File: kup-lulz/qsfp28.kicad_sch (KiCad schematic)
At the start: 33 parts, among them J15 CONN_QSFP_HOST, J16 CONN_QSFP_HOST, J35 QSFP_CAGE, J36 QSFP_CAGE, U9 XILINX_ULTRASCALEPLUS_B676

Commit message: Continued initial work on kup-lulz devboard
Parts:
- C81, C82: footprint (none) -> azonenberg_pcb:EIA_0402_CAP_NOSILK
- TP18, TP19, TP20, TP21, TP22, TP23: footprint (none) -> azonenberg_pcb:CONN_U.FL_TE_1909763-1
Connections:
- net QSFP28A_REFCLK0_N: no longer names the net of U9.K6 (MGTREFCLK0N_227)
- net QSFP28A_REFCLK0_P: no longer names the net of U9.K7 (MGTREFCLK0P_227)
- net QSFP28B_REFCLK0_N: no longer names the net of U9.P6 (MGTREFCLK0N_226)
- net QSFP28B_REFCLK0_P: no longer names the net of U9.P7 (MGTREFCLK0P_226)
- net QSFP28B_REFCLK1_N: no longer names the net of U9.M6 (MGTREFCLK1N_226)
- net QSFP28B_REFCLK1_P: no longer names the net of U9.M7 (MGTREFCLK1P_226)
- no-connect marks 0 -> 6
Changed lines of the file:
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@@
   (title_block
     (title "Kintex Ultrascale+ OshPark For The Lulz")
-    (date "2024-01-31")
+    (date "2024-02-01")
     (rev "0.1")
   )
@@
   (junction (at 48.26 135.89) (diameter 0) (color 0 0 0 0)
   )
+  (no_connect (at 138.43 26.67))
+  (no_connect (at 138.43 29.21))
+  (no_connect (at 48.26 19.05))
+  (no_connect (at 138.43 19.05))
+  (no_connect (at 48.26 21.59))
+  (no_connect (at 138.43 21.59))
   (wire (pts (xy 138.43 129.54) (xy 138.43 132.08))
     (stroke (width 0) (type default) (color 0 0 0 0))
@@
     (effects (font (size 1.27 1.27)) (justify left))
   )
-  (hierarchical_label "QSFP28B_REFCLK1_N" (shape input) (at 138.43 29.21 180)
-    (effects (font (size 1.27 1.27)) (justify right))
-  )
   (hierarchical_label "QSFP0_RST_N" (shape input) (at 78.74 135.89 0)
     (effects (font (size 1.27 1.27)) (justify left))
@@
     (effects (font (size 1.27 1.27)) (justify left))
   )
-  (hierarchical_label "QSFP28B_REFCLK1_P" (shape input) (at 138.43 26.67 180)
-    (effects (font (size 1.27 1.27)) (justify right))
-  )
   (hierarchical_label "QSFP28A_REFCLK1_P" (shape input) (at 48.26 26.67 180)
     (effects (font (size 1.27 1.27)) (justify right))
   )
-  (hierarchical_label "QSFP28B_REFCLK0_P" (shape input) (at 138.43 19.05 180)
-    (effects (font (size 1.27 1.27)) (justify right))
-  )
-  (hierarchical_label "QSFP28A_REFCLK0_P" (shape input) (at 48.26 19.05 180)
-    (effects (font (size 1.27 1.27)) (justify right))
-  )
   (hierarchical_label "QSFP_I2C_SDA" (shape bidirectional) (at 78.74 123.19 0)
     (effects (font (size 1.27 1.27)) (justify left))
   )
-  (hierarchical_label "QSFP28B_REFCLK0_N" (shape input) (at 138.43 21.59 180)
-    (effects (font (size 1.27 1.27)) (justify right))
-  )
   (hierarchical_label "GND" (shape input) (at 54.61 212.09 180)
     (effects (font (size 1.27 1.27)) (justify right))
@@
   (hierarchical_label "QSFP0_I2C_SEL_N" (shape input) (at 78.74 133.35 0)
     (effects (font (size 1.27 1.27)) (justify left))
-  )
-  (hierarchical_label "QSFP28A_REFCLK0_N" (shape input) (at 48.26 21.59 180)
-    (effects (font (size 1.27 1.27)) (justify right))
   )
   (hierarchical_label "QSFP1_LPMODE" (shape input) (at 168.91 129.54 0)
@@
       (effects (font (size 1.27 1.27)) (justify left))
     )
-    (property "Footprint" "" (id 2) (at 130.81 204.47 0)
+    (property "Footprint" "azonenberg_pcb:CONN_U.FL_TE_1909763-1" (id 2) (at 130.81 204.47 0)
       (effects (font (size 1.27 1.27)) hide)
     )
@@
       (effects (font (size 1.27 1.27)) (justify left))
     )
-    (property "Footprint" "" (id 2) (at 130.81 256.54 0)
+    (property "Footprint" "azonenberg_pcb:CONN_U.FL_TE_1909763-1" (id 2) (at 130.81 256.54 0)
       (effects (font (size 1.27 1.27)) hide)
     )
@@
       (effects (font (size 1.27 1.27)) (justify left))
     )
-    (property "Footprint" "" (id 2) (at 130.81 269.24 0)
+    (property "Footprint" "azonenberg_pcb:CONN_U.FL_TE_1909763-1" (id 2) (at 130.81 269.24 0)
       (effects (font (size 1.27 1.27)) hide)
     )
@@
       (effects (font (size 1.27 1.27)) (justify left))
     )
-    (property "Footprint" "" (id 2) (at 130.81 229.87 0)
+    (property "Footprint" "azonenberg_pcb:CONN_U.FL_TE_1909763-1" (id 2) (at 130.81 229.87 0)
       (effects (font (size 1.27 1.27)) hide)
     )
@@
       (effects (font (size 1.27 1.27)) (justify left))
     )
-    (property "Footprint" "" (id 2) (at 68.2752 212.09 0)
+    (property "Footprint" "azonenberg_pcb:EIA_0402_CAP_NOSILK" (id 2) (at 68.2752 212.09 0)
       (effects (font (size 1.27 1.27)) hide)
     )
@@
       (effects (font (size 1.27 1.27)) (justify left))
     )
-    (property "Footprint" "" (id 2) (at 68.2752 251.46 0)
+    (property "Footprint" "azonenberg_pcb:EIA_0402_CAP_NOSILK" (id 2) (at 68.2752 251.46 0)
       (effects (font (size 1.27 1.27)) hide)
     )
@@
       (effects (font (size 1.27 1.27)) (justify left))
     )
-    (property "Footprint" "" (id 2) (at 130.81 217.17 0)
+    (property "Footprint" "azonenberg_pcb:CONN_U.FL_TE_1909763-1" (id 2) (at 130.81 217.17 0)
       (effects (font (size 1.27 1.27)) hide)
     )
@@
       (effects (font (size 1.27 1.27)) (justify left))
     )
-    (property "Footprint" "" (id 2) (at 130.81 243.84 0)
-      (effects (font (size 1.27 1.27)) hide)
-    )
+    (property "Footprint" "azonenberg_pcb:CONN_U.FL_TE_1909763-1" (id 2) (at 130.81 243.84 0)
+      (effects (font (size 1.27 1.27)) hide)
+    )

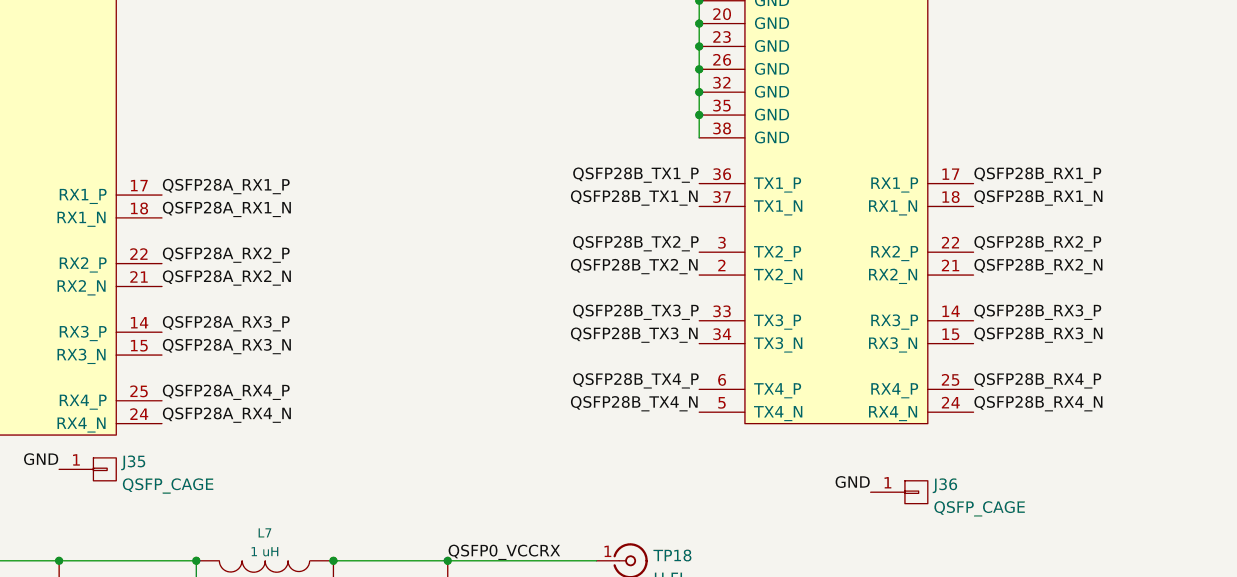
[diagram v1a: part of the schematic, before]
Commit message: Continued initial layout of kup-lulz
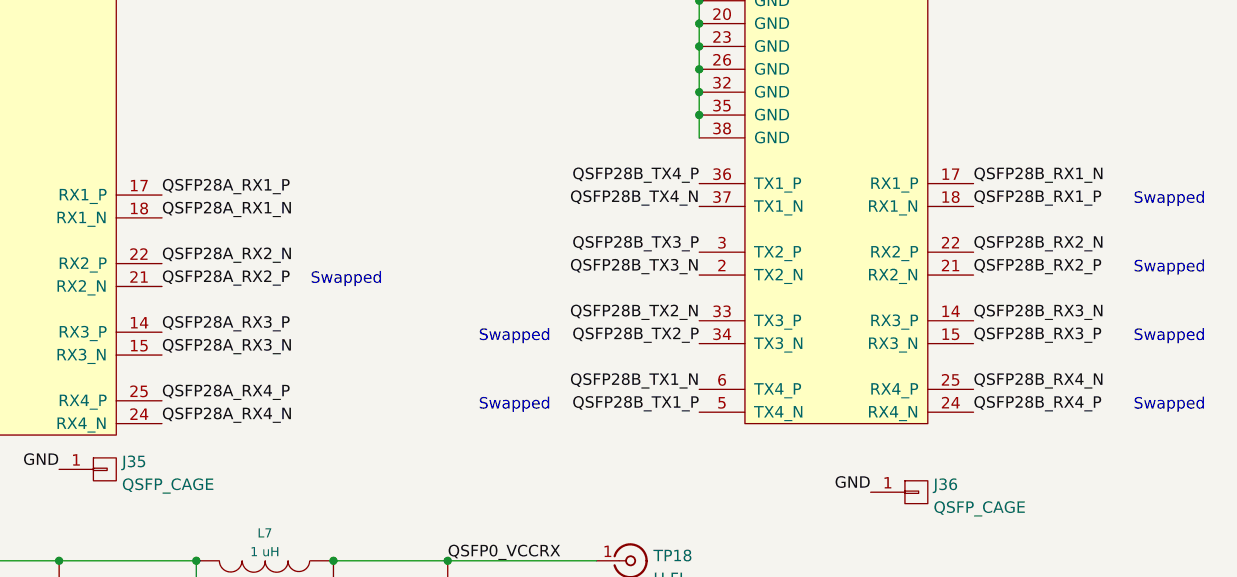
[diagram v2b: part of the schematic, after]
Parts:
- C79, C80, C83, C84, C85, C86, C87, C88: footprint (none) -> azonenberg_pcb:EIA_1210_CAP_NOSILK
- J15, J16: footprint azonenberg_pcb:CONN_QSFP+_TE_2110819-1 -> azonenberg_pcb:CONN_ZQSFP+_TE_1551920-2
- J35, J36: footprint azonenberg_pcb:CONN_QSFP_CAGE_TE_2110487-1 -> azonenberg_pcb:CONN_ZQSFP+_CAGE_TE_4-2170705-5
- L10, L11, L12, L7, L8, L9: footprint (none) -> azonenberg_pcb:EIA_0805_INDUCTOR_NOSILK
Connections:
- net QSFP28A_RX2_N: now also J15.22 (RX2_P); no longer J15.21 (RX2_N)
- net QSFP28A_RX2_P: now also J15.21 (RX2_N); no longer J15.22 (RX2_P)
- net QSFP28B_RX1_N: now also J16.17 (RX1_P); no longer J16.18 (RX1_N)
- net QSFP28B_RX1_P: now also J16.18 (RX1_N); no longer J16.17 (RX1_P)
- net QSFP28B_RX2_N: now also J16.22 (RX2_P); no longer J16.21 (RX2_N)
- net QSFP28B_RX2_P: now also J16.21 (RX2_N); no longer J16.22 (RX2_P)
- net QSFP28B_RX3_N: now also J16.14 (RX3_P); no longer J16.15 (RX3_N)
- net QSFP28B_RX3_P: now also J16.15 (RX3_N); no longer J16.14 (RX3_P)
- net QSFP28B_RX4_N: now also J16.25 (RX4_P); no longer J16.24 (RX4_N)
- net QSFP28B_RX4_P: now also J16.24 (RX4_N); no longer J16.25 (RX4_P)
- net QSFP28B_TX1_N: now also J16.6 (TX4_P); no longer J16.37 (TX1_N)
- net QSFP28B_TX1_P: now also J16.5 (TX4_N); no longer J16.36 (TX1_P)
- net QSFP28B_TX2_N: now also J16.33 (TX3_P); no longer J16.2 (TX2_N)
- net QSFP28B_TX2_P: now also J16.34 (TX3_N); no longer J16.3 (TX2_P)
- net QSFP28B_TX3_N: now also J16.2 (TX2_N); no longer J16.34 (TX3_N)
- net QSFP28B_TX3_P: now also J16.3 (TX2_P); no longer J16.33 (TX3_P)
- net QSFP28B_TX4_N: now also J16.37 (TX1_N); no longer J16.5 (TX4_N)
- net QSFP28B_TX4_P: now also J16.36 (TX1_P); no longer J16.6 (TX4_P)
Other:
- note added: "Swapped"
- company: (none) -> Antikernel Labs

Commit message: Continued initial layout
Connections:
- net QSFP28A_RX1_N: now also J15.22 (RX2_P); no longer J15.18 (RX1_N)
- net QSFP28A_RX1_P: now also J15.21 (RX2_N); no longer J15.17 (RX1_P)
- net QSFP28A_RX2_N: now also J15.17 (RX1_P); no longer J15.22 (RX2_P)
- net QSFP28A_RX2_P: now also J15.18 (RX1_N); no longer J15.21 (RX2_N)
- net QSFP28B_TX3_N: now also J16.3 (TX2_P); no longer J16.2 (TX2_N)
- net QSFP28B_TX3_P: now also J16.2 (TX2_N); no longer J16.3 (TX2_P)
- net QSFP28B_TX4_N: now also J16.36 (TX1_P); no longer J16.37 (TX1_N)
- net QSFP28B_TX4_P: now also J16.37 (TX1_N); no longer J16.36 (TX1_P)
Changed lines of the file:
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@@
     (stroke (width 0) (type default) (color 0 0 0 0))
   )
+  (text "Swapped" (at 121.92 165.1 180)
+    (effects (font (size 1.27 1.27)) (justify right bottom))
+  )
+  (text "Swapped" (at 121.92 172.72 180)
+    (effects (font (size 1.27 1.27)) (justify right bottom))
+  )
   (text "Swapped" (at 186.69 172.72 0)
     (effects (font (size 1.27 1.27)) (justify left bottom))
@@
     (effects (font (size 1.27 1.27)) (justify left bottom))
   )
+  (text "Swapped" (at 95.25 166.37 0)
+    (effects (font (size 1.27 1.27)) (justify left bottom))
+  )
   (text "Swapped" (at 121.92 180.34 180)
     (effects (font (size 1.27 1.27)) (justify right bottom))
@@
     (effects (font (size 1.27 1.27)) (justify left bottom))
   )
-  (label "QSFP28A_RX1_P" (at 78.74 163.83 0)
+  (label "QSFP28A_RX1_P" (at 78.74 173.99 0)
     (effects (font (size 1.27 1.27)) (justify left bottom))
   )
@@
     (effects (font (size 1.27 1.27)) (justify right bottom))
   )
-  (label "QSFP28A_RX2_N" (at 78.74 171.45 0)
+  (label "QSFP28A_RX2_N" (at 78.74 163.83 0)
     (effects (font (size 1.27 1.27)) (justify left bottom))
   )
@@
     (effects (font (size 1.27 1.27)) (justify left bottom))
   )
-  (label "QSFP28B_TX4_N" (at 138.43 165.1 180)
-    (effects (font (size 1.27 1.27)) (justify right bottom))
-  )
-  (label "QSFP28A_RX2_P" (at 78.74 173.99 0)
+  (label "QSFP28B_TX4_N" (at 138.43 162.56 180)
+    (effects (font (size 1.27 1.27)) (justify right bottom))
+  )
+  (label "QSFP28A_RX2_P" (at 78.74 166.37 0)
     (effects (font (size 1.27 1.27)) (justify left bottom))
   )
@@
     (effects (font (size 1.27 1.27)) (justify right bottom))
   )
-  (label "QSFP28B_TX3_N" (at 138.43 172.72 180)
+  (label "QSFP28B_TX3_N" (at 138.43 170.18 180)
     (effects (font (size 1.27 1.27)) (justify right bottom))
   )
@@
     (effects (font (size 1.27 1.27)) (justify right bottom))
   )
-  (label "QSFP28A_RX1_N" (at 78.74 166.37 0)
+  (label "QSFP28A_RX1_N" (at 78.74 171.45 0)
     (effects (font (size 1.27 1.27)) (justify left bottom))
   )
@@
     (effects (font (size 1.27 1.27)) (justify right bottom))
   )
-  (label "QSFP28B_TX3_P" (at 138.43 170.18 180)
+  (label "QSFP28B_TX3_P" (at 138.43 172.72 180)
     (effects (font (size 1.27 1.27)) (justify right bottom))
   )
@@
     (effects (font (size 1.27 1.27)) (justify right bottom))
   )
-  (label "QSFP28B_TX4_P" (at 138.43 162.56 180)
-    (effects (font (size 1.27 1.27)) (justify right bottom))
-  )
+  (label "QSFP28B_TX4_P" (at 138.43 165.1 180)
+    (effects (font (size 1.27 1.27)) (justify right bottom))
+  )

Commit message: Continued initial routing
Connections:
- net QSFP28A_RX2_N: now also J15.18 (RX1_N); no longer J15.17 (RX1_P)
- net QSFP28A_RX2_P: now also J15.17 (RX1_P); no longer J15.18 (RX1_N)
- net QSFP28A_RX3_N: now also J15.25 (RX4_P); no longer J15.15 (RX3_N)
- net QSFP28A_RX3_P: now also J15.24 (RX4_N); no longer J15.14 (RX3_P)
- net QSFP28A_RX4_N: now also J15.15 (RX3_N); no longer J15.24 (RX4_N)
- net QSFP28A_RX4_P: now also J15.14 (RX3_P); no longer J15.25 (RX4_P)
- net QSFP28A_TX2_N: now also J15.33 (TX3_P); no longer J15.2 (TX2_N)
- net QSFP28A_TX2_P: now also J15.34 (TX3_N); no longer J15.3 (TX2_P)
- net QSFP28A_TX3_N: now also J15.6 (TX4_P); no longer J15.34 (TX3_N)
- net QSFP28A_TX3_P: now also J15.5 (TX4_N); no longer J15.33 (TX3_P)
- net QSFP28A_TX4_N: now also J15.3 (TX2_P); no longer J15.5 (TX4_N)
- net QSFP28A_TX4_P: now also J15.2 (TX2_N); no longer J15.6 (TX4_P)
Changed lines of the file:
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@@
     (stroke (width 0) (type default) (color 0 0 0 0))
   )
+  (text "Swapped" (at 31.75 181.61 180)
+    (effects (font (size 1.27 1.27)) (justify right bottom))
+  )
   (text "Swapped" (at 121.92 165.1 180)
     (effects (font (size 1.27 1.27)) (justify right bottom))
@@
     (effects (font (size 1.27 1.27)) (justify right bottom))
   )
+  (text "Swapped" (at 31.75 187.96 180)
+    (effects (font (size 1.27 1.27)) (justify right bottom))
+  )
   (text "Swapped" (at 186.69 172.72 0)
     (effects (font (size 1.27 1.27)) (justify left bottom))
@@
     (effects (font (size 1.27 1.27)) (justify left bottom))
   )
+  (text "Swapped" (at 95.25 187.96 0)
+    (effects (font (size 1.27 1.27)) (justify left bottom))
+  )
   (text "Swapped" (at 95.25 173.99 0)
     (effects (font (size 1.27 1.27)) (justify left bottom))
   )
-  (text "Swapped" (at 95.25 166.37 0)
-    (effects (font (size 1.27 1.27)) (justify left bottom))
-  )
   (text "Swapped" (at 121.92 180.34 180)
     (effects (font (size 1.27 1.27)) (justify right bottom))
@@
     (effects (font (size 1.27 1.27)) (justify left bottom))
   )
-  (label "QSFP28A_RX4_P" (at 78.74 186.69 0)
+  (label "QSFP28A_RX4_P" (at 78.74 179.07 0)
     (effects (font (size 1.27 1.27)) (justify left bottom))
   )
@@
     (effects (font (size 1.27 1.27)) (justify right bottom))
   )
-  (label "QSFP28A_RX3_N" (at 78.74 181.61 0)
+  (label "QSFP28A_RX3_N" (at 78.74 186.69 0)
     (effects (font (size 1.27 1.27)) (justify left bottom))
   )
@@
     (effects (font (size 1.27 1.27)) (justify right bottom))
   )
-  (label "QSFP28A_TX4_N" (at 48.26 189.23 180)
+  (label "QSFP28A_TX4_N" (at 48.26 171.45 180)
     (effects (font (size 1.27 1.27)) (justify right bottom))
   )
@@
     (effects (font (size 1.27 1.27)) (justify right bottom))
   )
-  (label "QSFP28A_TX2_P" (at 48.26 171.45 180)
+  (label "QSFP28A_TX2_P" (at 48.26 181.61 180)
     (effects (font (size 1.27 1.27)) (justify right bottom))
   )
@@
     (effects (font (size 1.27 1.27)) (justify right bottom))
   )
-  (label "QSFP28A_TX3_P" (at 48.26 179.07 180)
+  (label "QSFP28A_TX3_P" (at 48.26 189.23 180)
     (effects (font (size 1.27 1.27)) (justify right bottom))
   )
@@
     (effects (font (size 1.27 1.27)) (justify right bottom))
   )
-  (label "QSFP28A_RX2_N" (at 78.74 163.83 0)
+  (label "QSFP28A_RX2_N" (at 78.74 166.37 0)
     (effects (font (size 1.27 1.27)) (justify left bottom))
   )
@@
     (effects (font (size 1.27 1.27)) (justify right bottom))
   )
-  (label "QSFP28A_RX2_P" (at 78.74 166.37 0)
+  (label "QSFP28A_RX2_P" (at 78.74 163.83 0)
     (effects (font (size 1.27 1.27)) (justify left bottom))
   )
@@
     (effects (font (size 1.27 1.27)) (justify right bottom))
   )
-  (label "QSFP28A_TX4_P" (at 48.26 186.69 180)
+  (label "QSFP28A_TX4_P" (at 48.26 173.99 180)
     (effects (font (size 1.27 1.27)) (justify right bottom))
   )
@@
     (effects (font (size 1.27 1.27)) (justify right bottom))
   )
-  (label "QSFP28A_TX3_N" (at 48.26 181.61 180)
-    (effects (font (size 1.27 1.27)) (justify right bottom))
-  )
-  (label "QSFP28A_RX3_P" (at 78.74 179.07 0)
-    (effects (font (size 1.27 1.27)) (justify left bottom))
-  )
-  (label "QSFP28A_RX4_N" (at 78.74 189.23 0)
+  (label "QSFP28A_TX3_N" (at 48.26 186.69 180)
+    (effects (font (size 1.27 1.27)) (justify right bottom))
+  )
+  (label "QSFP28A_RX3_P" (at 78.74 189.23 0)
+    (effects (font (size 1.27 1.27)) (justify left bottom))
+  )
+  (label "QSFP28A_RX4_N" (at 78.74 181.61 0)
     (effects (font (size 1.27 1.27)) (justify left bottom))
   )
@@
     (effects (font (size 1.27 1.27)) (justify right bottom))
   )
-  (label "QSFP28A_TX2_N" (at 48.26 173.99 180)
-    (effects (font (size 1.27 1.27)) (justify right bottom))
-  )
+  (label "QSFP28A_TX2_N" (at 48.26 179.07 180)
+    (effects (font (size 1.27 1.27)) (justify right bottom))
+  )

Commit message: Continued kup-lulz routing. Deleted one of the PMODs as there's no way it will fit.
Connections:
- net QSFP28A_TX1_N: now also J15.3 (TX2_P); no longer J15.37 (TX1_N)
- net QSFP28A_TX1_P: now also J15.2 (TX2_N); no longer J15.36 (TX1_P)
- net QSFP28A_TX3_N: now also J15.36 (TX1_P); no longer J15.6 (TX4_P)
- net QSFP28A_TX3_P: now also J15.37 (TX1_N); no longer J15.5 (TX4_N)
- net QSFP28A_TX4_N: now also J15.6 (TX4_P); no longer J15.3 (TX2_P)
- net QSFP28A_TX4_P: now also J15.5 (TX4_N); no longer J15.2 (TX2_N)
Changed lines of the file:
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@@
   (title_block
     (title "Kintex Ultrascale+ OshPark For The Lulz")
-    (date "2024-02-05")
+    (date "2024-02-06")
     (rev "0.1")
     (company "Antikernel Labs")
@@
     (effects (font (size 1.27 1.27)) (justify right bottom))
   )
+  (text "Swapped" (at 31.75 173.99 180)
+    (effects (font (size 1.27 1.27)) (justify right bottom))
+  )
   (text "Swapped" (at 186.69 172.72 0)
     (effects (font (size 1.27 1.27)) (justify left bottom))
@@
     (effects (font (size 1.27 1.27)) (justify left bottom))
   )
+  (text "Swapped" (at 31.75 166.37 180)
+    (effects (font (size 1.27 1.27)) (justify right bottom))
+  )
   (text "Swapped" (at 121.92 180.34 180)
     (effects (font (size 1.27 1.27)) (justify right bottom))
@@
     (effects (font (size 1.27 1.27)) (justify right bottom))
   )
-  (label "QSFP28A_TX4_N" (at 48.26 171.45 180)
+  (label "QSFP28A_TX4_N" (at 48.26 186.69 180)
     (effects (font (size 1.27 1.27)) (justify right bottom))
   )
@@
     (effects (font (size 1.27 1.27)) (justify left bottom))
   )
-  (label "QSFP28A_TX1_N" (at 48.26 166.37 180)
+  (label "QSFP28A_TX1_N" (at 48.26 171.45 180)
     (effects (font (size 1.27 1.27)) (justify right bottom))
   )
@@
     (effects (font (size 1.27 1.27)) (justify right bottom))
   )
-  (label "QSFP28A_TX3_P" (at 48.26 189.23 180)
+  (label "QSFP28A_TX3_P" (at 48.26 166.37 180)
     (effects (font (size 1.27 1.27)) (justify right bottom))
   )
@@
     (effects (font (size 1.27 1.27)) (justify right bottom))
   )
-  (label "QSFP28A_TX4_P" (at 48.26 173.99 180)
+  (label "QSFP28A_TX4_P" (at 48.26 189.23 180)
     (effects (font (size 1.27 1.27)) (justify right bottom))
   )
@@
     (effects (font (size 1.27 1.27)) (justify right bottom))
   )
-  (label "QSFP28A_TX1_P" (at 48.26 163.83 180)
+  (label "QSFP28A_TX1_P" (at 48.26 173.99 180)
     (effects (font (size 1.27 1.27)) (justify right bottom))
   )
@@
     (effects (font (size 1.27 1.27)) (justify right bottom))
   )
-  (label "QSFP28A_TX3_N" (at 48.26 186.69 180)
-    (effects (font (size 1.27 1.27)) (justify right bottom))
-  )
+  (label "QSFP28A_TX3_N" (at 48.26 163.83 180)
+    (effects (font (size 1.27 1.27)) (justify right bottom))
+  )
